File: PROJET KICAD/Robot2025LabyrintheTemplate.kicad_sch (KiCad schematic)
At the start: 34 parts, among them J1 HC-SR04 gauche, J11 SERVO MOTEUR 4, J12 Conn_01x06_Pin, J13 Conn_01x05_Pin, J14 Conn_01x02_Pin, J15 CON 1x2 POLARIZED, J16 Conn_01x05_Pin, J17 Conn_01x04_Pin, J18 Conn_01x02_Pin, J19 Conn_01x04_Pin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

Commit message: fin de la schematique, debut rotage
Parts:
- removed J12, J6: Conn_01x06_Pin, ISI-Connector_PinHeader_2.54mm:PinHeader_1x06_P2.54mm_Long_Vertical, symbol ISI-Connector_PinHeader_2.54mm:Conn_01x06_Pin
- removed J19: Conn_01x04_Pin, ISI-Connector_JST:JST_XH_B4B-XH-AM_1x04_P2.50mm_Long_Vertical, symbol ISI-Connector_JST:Conn_01x04_Pin
- removed J5: cap sen0101, ISI-Connector_PinSocket_2.54mm:PinSocket_2x04_P2.54mm_Vertical, symbol ISI-Connector_PinSocket_2.54mm:Conn_02x04_Odd_Even
- added J2, J6: cap sen0101, ISI-Connector_JST:JST_XH_B4B-XH-AM_1x04_P2.50mm_Long_Vertical, symbol ISI-Connector_JST:Conn_01x04_Pin
- added J20, J22: Conn_01x04_Pin, ISI-Connector_JST:JST_XH_B4B-XH-AM_1x04_P2.50mm_Long_Vertical, symbol ISI-Connector_JST:Conn_01x04_Pin
- added J21: moteur 3, ISI-Connector_JST:JST_XH_B4B-XH-AM_1x04_P2.50mm_Long_Vertical, symbol ISI-Connector_JST:Conn_01x04_Pin
- J13: value Conn_01x05_Pin -> capteur TOF BAS
- J14: value Conn_01x02_Pin -> Vinput regul
- J16: value Conn_01x05_Pin -> capteur TOF HAUT
- J18: value Conn_01x02_Pin -> Vout regul
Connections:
- net +5V: now also J11.2 (Pin_2), J4.2 (Pin_2), J7.2 (Pin_2), J2.3 (Pin_3); no longer A3.10 (M0), A3.11 (M1), A3.12 (M2), A4.10 (M0), A4.11 (M1), A4.12 (M2)
- net D_OUT: now also J2.2 (Pin_2)
- net D_S0: now also J6.1 (Pin_1)
- net D_S1: now also J6.2 (Pin_2)
- net D_S2: now also J6.3 (Pin_3)
- net D_S3: now also J6.4 (Pin_4)
- net GND: now also A1.7 (GND), A3.10 (M0), A3.11 (M1), A3.12 (M2), A3.7 (GND), A4.10 (M0), A4.11 (M1), A4.12 (M2), A4.7 (GND), J2.1 (Pin_1), J2.4 (Pin_4)
- net Vin: now also A1.8 (VMOT), A3.8 (VMOT), A4.8 (VMOT)
- net at A5.4 (A1), J17.1 (Pin_1): no longer A5.3 (A2)
- net at J17.2 (Pin_2): now also A5.3 (A2)
- net at A1.3 (A2): now also J20.2 (Pin_2)
- net at A1.4 (A1): now also J20.1 (Pin_1)
- net at A1.5 (B1): now also J20.3 (Pin_3)
- net at A1.6 (B2): now also J20.4 (Pin_4)
- net at A3.3 (A2): now also J21.2 (Pin_2)
- net at A3.4 (A1): now also J21.1 (Pin_1)
- net at A3.5 (B1): now also J21.3 (Pin_3)
- net at A3.6 (B2): now also J21.4 (Pin_4)
- net at A4.3 (A2): now also J22.2 (Pin_2)
- net at A4.4 (A1): now also J22.1 (Pin_1)
- net at A4.5 (B1): now also J22.3 (Pin_3)
- net at A4.6 (B2): now also J22.4 (Pin_4)
- no-connect marks 59 -> 56
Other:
- note removed: "GND"
- note removed: "VIN"
- moved on the sheet: C1, C2, C4, J14, J17, J18, U2, U4

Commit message: routage 1
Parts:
- J17: value Conn_01x04_Pin -> moteur 2 AV
- J20: value Conn_01x04_Pin -> moteur 3 DR
- J21: value moteur 3 -> moteur 4 DR
- J22: value Conn_01x04_Pin -> moteur 1 AV
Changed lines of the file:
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@@
 			)
 		)
-		(property "Value" "Conn_01x04_Pin"
+		(property "Value" "moteur 2 AV"
 			(at 64.77 104.14 0)
 			(show_name no)
@@
 			)
 		)
-		(property "Value" "moteur 3"
+		(property "Value" "moteur 4 DR"
 			(at 231.14 128.27 0)
 			(show_name no)
@@
 			)
 		)
-		(property "Value" "Conn_01x04_Pin"
+		(property "Value" "moteur 3 DR"
 			(at 238.76 88.9 0)
 			(show_name no)
@@
 			)
 		)
-		(property "Value" "Conn_01x04_Pin"
+		(property "Value" "moteur 1 AV"
 			(at 146.05 161.29 0)
 			(show_name no)

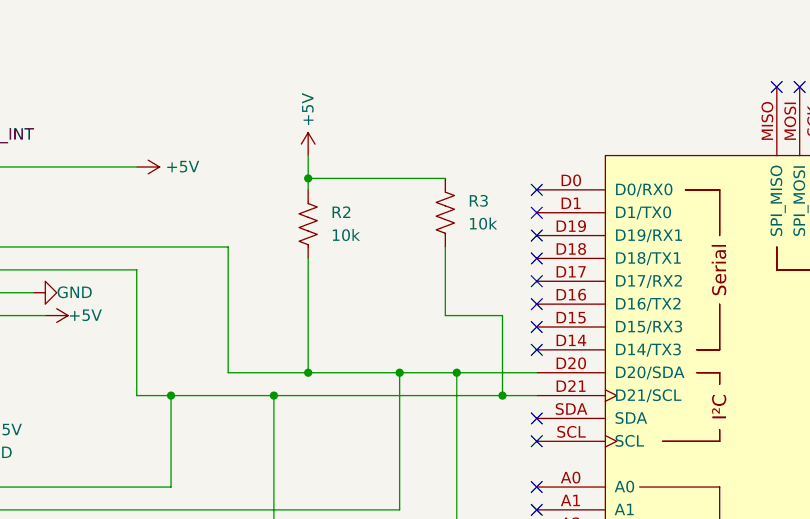
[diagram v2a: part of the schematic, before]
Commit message: gnd et 5v
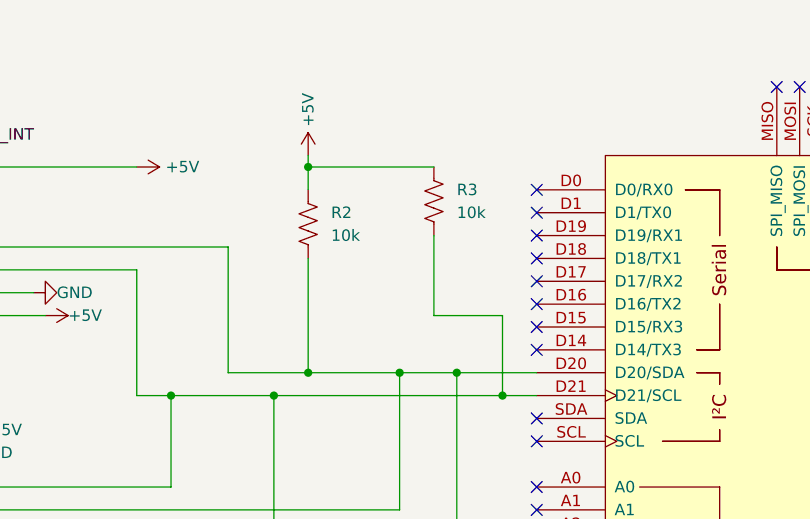
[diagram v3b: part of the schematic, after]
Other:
- moved on the sheet: R3
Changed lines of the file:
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@@
 	)
 	(junction
-		(at 101.6 121.92)
+		(at 78.74 30.48)
 		(diameter 0)
 		(color 0 0 0 0)
 	)
 	(junction
-		(at 72.39 167.64)
+		(at 101.6 121.92)
 		(diameter 0)
 		(color 0 0 0 0)
 	)
 	(junction
-		(at 212.09 120.65)
+		(at 72.39 167.64)
 		(diameter 0)
 		(color 0 0 0 0)
 	)
 	(junction
-		(at 125.73 193.04)
+		(at 212.09 120.65)
 		(diameter 0)
 		(color 0 0 0 0)
 	)
 	(junction
-		(at 78.74 31.75)
+		(at 125.73 193.04)
 		(diameter 0)
 		(color 0 0 0 0)
@@
 	(wire
 		(pts
-			(xy 78.74 29.21) (xy 78.74 31.75)
+			(xy 78.74 29.21) (xy 78.74 30.48)
 		)
 		(stroke
@@
 	(wire
 		(pts
-			(xy 93.98 31.75) (xy 78.74 31.75)
+			(xy 92.71 30.48) (xy 78.74 30.48)
 		)
 		(stroke
@@
 	(wire
 		(pts
-			(xy 93.98 46.99) (xy 100.33 46.99)
+			(xy 92.71 46.99) (xy 100.33 46.99)
 		)
 		(stroke
@@
 	(wire
 		(pts
-			(xy 78.74 31.75) (xy 78.74 33.02)
-		)
-		(stroke
-			(width 0)
-			(type default)
-		)
-	)
-	(wire
-		(pts
 			(xy 189.23 22.86) (xy 193.04 22.86)
 		)
@@
 	(wire
 		(pts
+			(xy 78.74 30.48) (xy 78.74 33.02)
+		)
+		(stroke
+			(width 0)
+			(type default)
+		)
+	)
+	(wire
+		(pts
 			(xy 220.98 193.04) (xy 228.6 193.04)
 		)
@@
 	(wire
 		(pts
-			(xy 93.98 39.37) (xy 93.98 46.99)
+			(xy 92.71 38.1) (xy 92.71 46.99)
 		)
 		(stroke
@@
 	(symbol
 		(lib_id "ISI-Resistor:R_US_1206")
-		(at 93.98 35.56 0)
+		(at 92.71 34.29 0)
 		(unit 1)
 		(body_style 1)
@@
 		(fields_autoplaced yes)
 		(property "Reference" "R3"
-			(at 96.52 34.2899 0)
+			(at 95.25 33.0199 0)
 			(show_name no)
 			(do_not_autoplace no)
@@
 		)
 		(property "Value" "10k"
-			(at 96.52 36.8299 0)
+			(at 95.25 35.5599 0)
 			(show_name no)
 			(do_not_autoplace no)
@@
 		)
 		(property "Footprint" "ISI-Resistor:R_1206_3216Metric_Pad1.30x1.75mm_HandSolder"
-			(at 94.996 35.814 90)
+			(at 93.726 34.544 90)
 			(hide yes)
 			(show_name no)
@@
 		)
 		(property "Datasheet" ""
-			(at 93.98 35.56 0)
+			(at 92.71 34.29 0)
 			(hide yes)
 			(show_name no)
@@
 		)
 		(property "Description" "Resistor, US symbol 1206 SMD"
-			(at 93.98 35.56 0)
+			(at 92.71 34.29 0)
 			(hide yes)
 			(show_name no)
@@
 		)
 		(property "PartNumber" "Voir farde de resistance"
-			(at 93.98 35.56 0)
+			(at 92.71 34.29 0)
 			(hide yes)
 			(show_name no)
@@
 		)
 		(property "Emplacement" "Voir farde de resistance"
-			(at 93.98 35.56 0)
+			(at 92.71 34.29 0)
 			(hide yes)
 			(show_name no)

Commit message: maj2
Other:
- moved on the sheet: C1, C2, C4, U2, U4

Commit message: Différentes modifs à discuter de vive voix
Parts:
- added R5, R6: 0R, ISI-Resistor:R_1206_3216Metric_Pad1.30x1.75mm_HandSolder, symbol ISI-Resistor:R_US_1206
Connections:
- net +5V: no longer A5.10 (M0), A5.11 (M1), A5.12 (M2)
- net D_CSN: now also R5.2, R6.2; no longer A2.D49
- net GND: now also A5.10 (M0), A5.11 (M1), A5.12 (M2)
- net at A2.D53 (D53_CS): now also R5.1
- new net: A2.D49, R6.1
- no-connect marks 56 -> 55
